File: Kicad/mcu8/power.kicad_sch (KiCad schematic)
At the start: 17 parts, among them IC201 TLV1117-50, K201 Battery, T201 DMP2305U, T202 DMP2305U

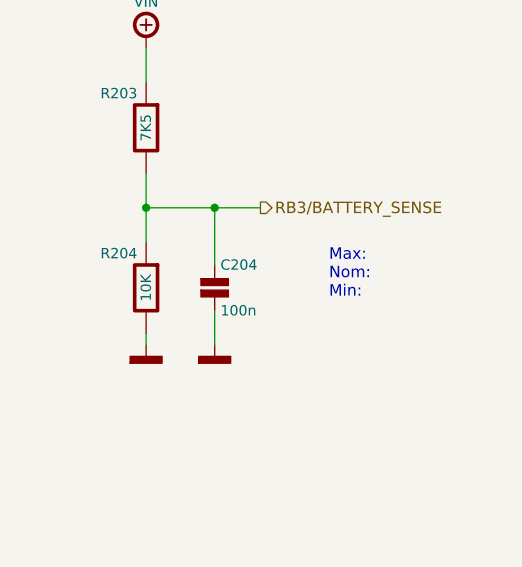
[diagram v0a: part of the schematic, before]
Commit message: Update MCU 8Bit
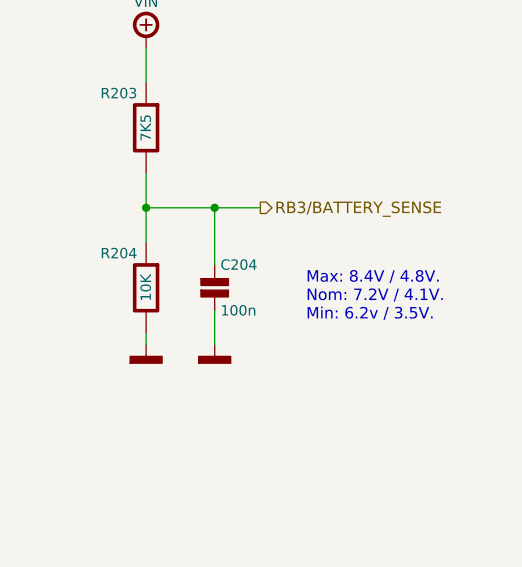
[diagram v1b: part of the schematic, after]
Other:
- note added: "Max: 8.4V / 4.8V. Nom: 7.2V / 4.1V. Min: 6.2v / 3.5V."
- note removed: "Max: Nom: Min:"
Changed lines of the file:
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@@
     (stroke (width 0) (type solid) (color 0 0 0 0))
   )
-  (text "Max:\nNom:\nMin:" (at 205.74 73.66 0)
+  (text "Max: 8.4V / 4.8V.\nNom: 7.2V / 4.1V.\nMin: 6.2v / 3.5V."
+    (at 203.2 76.2 0)
     (effects (font (size 1.27 1.27)) (justify left bottom))
   )
